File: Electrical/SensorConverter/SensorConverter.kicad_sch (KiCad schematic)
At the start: 35 parts, among them J1 1990067, J2 0430450600, J3 Conn_ARM_SWD_TagConnect_TC203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, U1 THVD1400DR, U2 LP2950CDTX-3.3/NOPB, U3 STM32F103T8U6, U4 M24M01E-FMC6TG

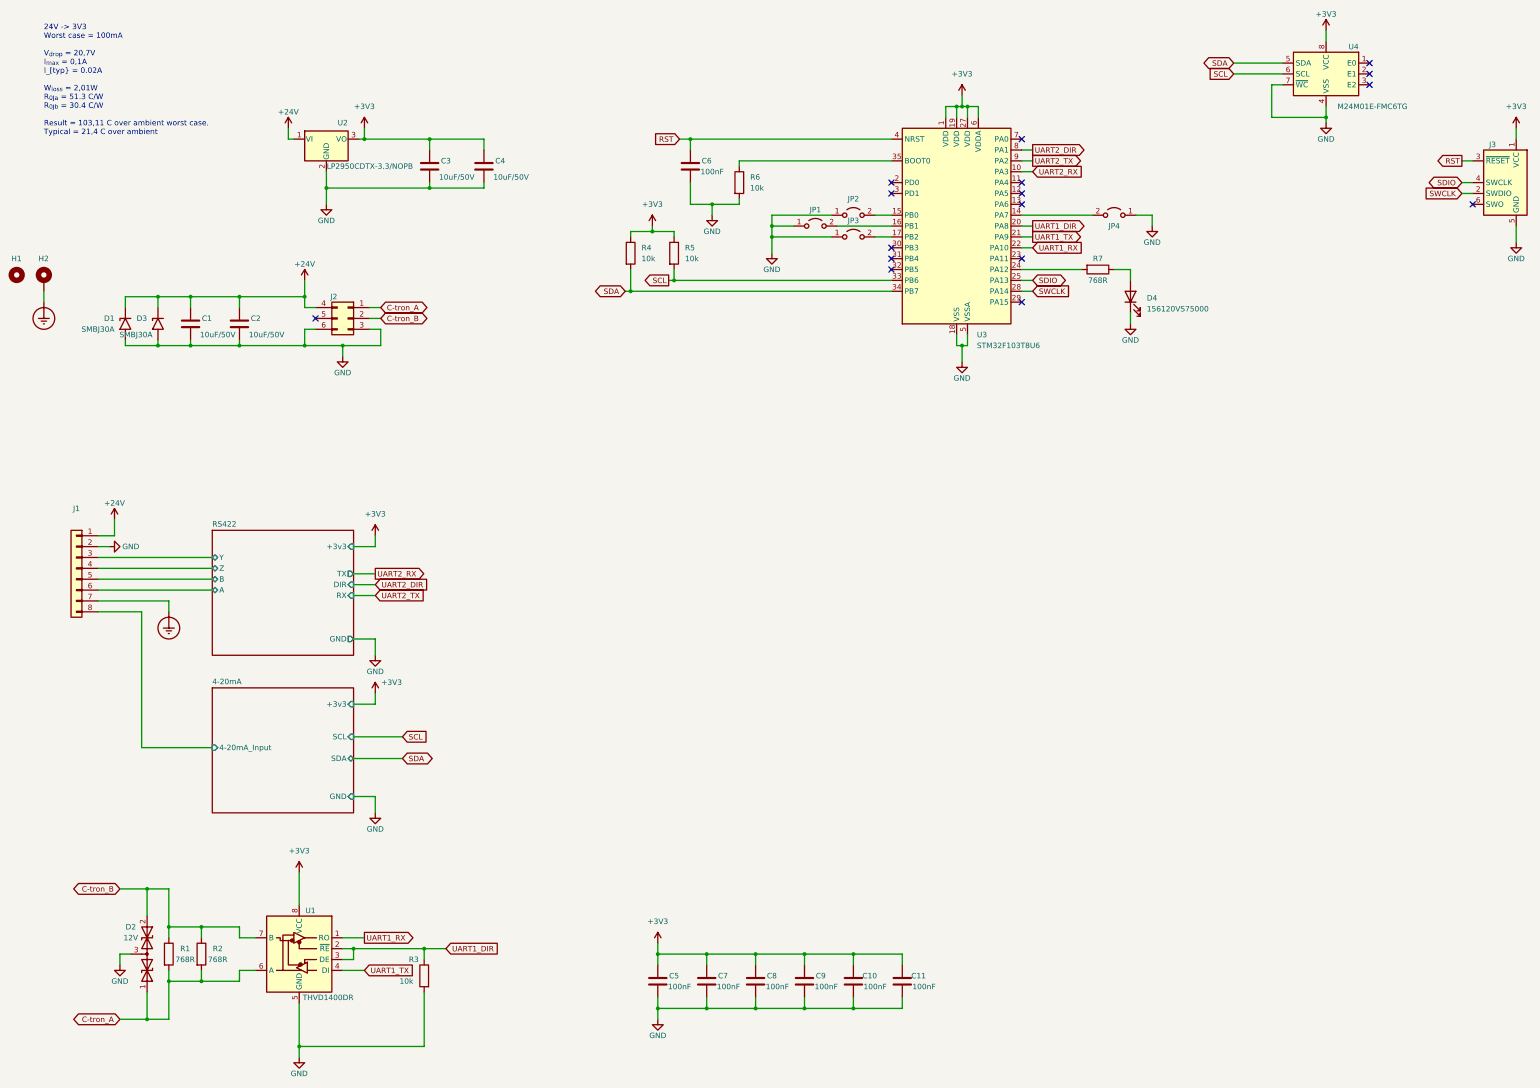
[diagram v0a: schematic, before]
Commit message: Changing processor to STM32G0
This is mostly because of memory constraints and that the F103 is having a lot of issue.
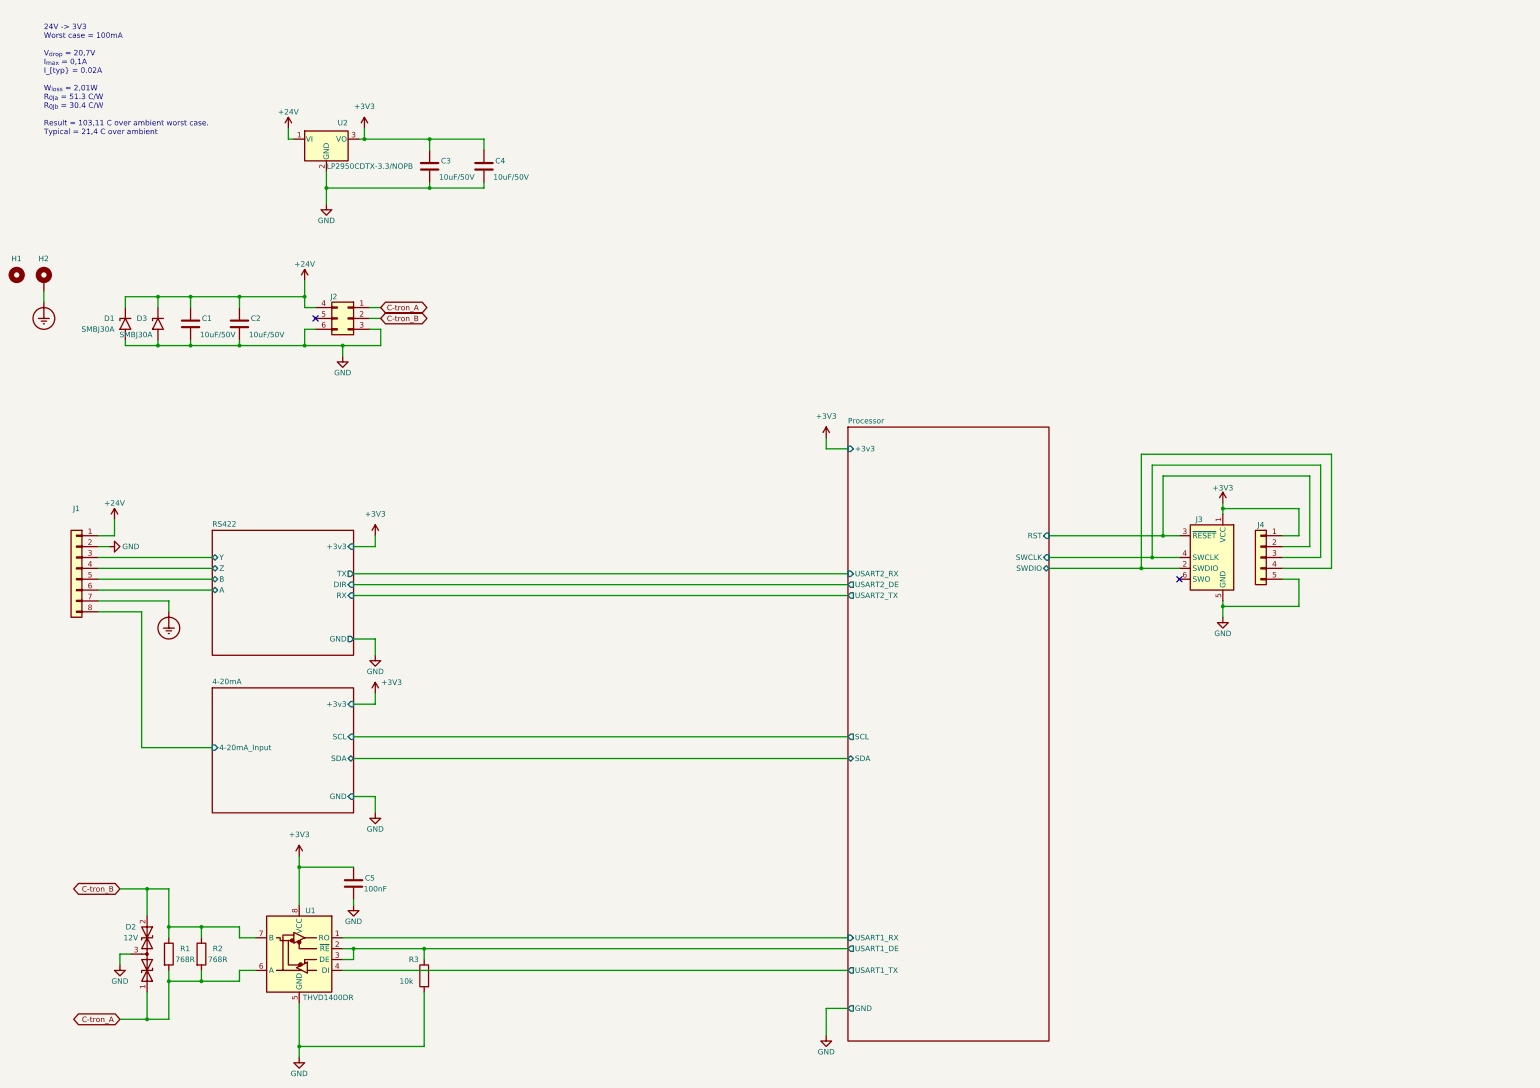
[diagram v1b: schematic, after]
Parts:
- removed C10, C11, C6, C7, C8, C9: 100nF, Capacitor_SMD:C_0402_1005Metric, symbol Device:C
- removed D4: 156120VS75000, LT600_Adapter:WL-SMRW, symbol Device:LED
- removed JP1, JP2, JP3, JP4: Jumper_2_Open, Jumper:SolderJumper-2_P1.3mm_Open_RoundedPad1.0x1.5mm, symbol Jumper:Jumper_2_Open
- removed R4, R5, R6: 10k, Resistor_SMD:R_0402_1005Metric, symbol Device:R
- removed R7: 768R, Resistor_SMD:R_0603_1608Metric, symbol Device:R
- removed U3: STM32F103T8U6, Package_DFN_QFN:QFN-36-1EP_6x6mm_P0.5mm_EP4.1x4.1mm, symbol MCU_ST_STM32F1:STM32F103T8Ux
- removed U4: M24M01E-FMC6TG, Package_DFN_QFN:DFN-8-1EP_3x2mm_P0.5mm_EP1.3x1.5mm, symbol Memory_EEPROM:M24C01-FMN
- added J4: Conn_01x05, Connector_PinHeader_1.27mm:PinHeader_1x05_P1.27mm_Vertical, symbol Connector_Generic:Conn_01x05
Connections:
- net +3V3: now also J4.1 (Pin_1)
- net GND: now also J4.5 (Pin_5)
- net RST renamed Processor/RST
- net Processor/RST: now also J4.2 (Pin_2)
- net SDIO renamed Processor/SWCLK
- net Processor/SWCLK: now also J4.3 (Pin_3)
- net SWCLK renamed Processor/SWDIO
- net Processor/SWDIO: now also J4.4 (Pin_4)
- net UART1_DIR renamed Processor/USART1_DE
- net UART1_RX renamed Processor/USART1_RX
- net UART1_TX renamed Processor/USART1_TX
- no-connect marks 16 -> 2
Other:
- added sheet Processor (STM32G0.kicad_sch)
- moved on the sheet: C5, J3

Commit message: Finalized PCB RevB
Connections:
- net Processor/SWCLK: now also J4.4 (Pin_4); no longer J4.3 (Pin_3)
- net Processor/SWDIO: now also J4.3 (Pin_3); no longer J4.4 (Pin_4)
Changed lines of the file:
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@@
+	)
+	(junction
+		(at 295.91 144.78)
+		(diameter 0)
+		(color 0 0 0 0)
 	)
 	(junction
@@
 	)
 	(junction
+		(at 298.45 147.32)
+		(diameter 0)
+		(color 0 0 0 0)
+	)
+	(junction
 		(at 68.58 231.14)
 		(diameter 0)
@@
 	(junction
 		(at 109.22 95.25)
-		(diameter 0)
-		(color 0 0 0 0)
-	)
-	(junction
-		(at 298.45 144.78)
-		(diameter 0)
-		(color 0 0 0 0)
-	)
-	(junction
-		(at 295.91 147.32)
 		(diameter 0)
 		(color 0 0 0 0)
@@
 	(wire
 		(pts
-			(xy 274.32 144.78) (xy 298.45 144.78)
+			(xy 274.32 144.78) (xy 295.91 144.78)
+		)
+		(stroke
+			(width 0)
+			(type default)
+		)
+	)
+	(wire
+		(pts
+			(xy 295.91 120.65) (xy 295.91 144.78)
 		)
 		(stroke
@@
 	(wire
 		(pts
-			(xy 295.91 120.65) (xy 295.91 147.32)
-		)
-		(stroke
-			(width 0)
-			(type default)
-		)
-	)
-	(wire
-		(pts
 			(xy 68.58 243.84) (xy 76.2 243.84)
 		)
@@
 	(wire
 		(pts
-			(xy 274.32 147.32) (xy 295.91 147.32)
-		)
-		(stroke
-			(width 0)
-			(type default)
-		)
-	)
-	(wire
-		(pts
 			(xy 335.28 142.24) (xy 335.28 125.73)
 		)
@@
 	(wire
 		(pts
-			(xy 298.45 144.78) (xy 304.8 144.78)
-		)
-		(stroke
-			(width 0)
-			(type default)
-		)
-	)
-	(wire
-		(pts
 			(xy 109.22 95.25) (xy 109.22 97.79)
 		)
@@
 	(wire
 		(pts
-			(xy 295.91 147.32) (xy 304.8 147.32)
+			(xy 274.32 147.32) (xy 298.45 147.32)
 		)
 		(stroke
@@
 	(wire
 		(pts
+			(xy 298.45 147.32) (xy 304.8 147.32)
+		)
+		(stroke
+			(width 0)
+			(type default)
+		)
+	)
+	(wire
+		(pts
 			(xy 328.93 149.86) (xy 332.74 149.86)
 		)
@@
 	(wire
 		(pts
-			(xy 298.45 144.78) (xy 298.45 123.19)
-		)
-		(stroke
-			(width 0)
-			(type default)
-		)
-	)
-	(wire
-		(pts
 			(xy 39.37 82.55) (xy 39.37 85.09)
 		)
@@
 	(wire
 		(pts
+			(xy 298.45 123.19) (xy 298.45 147.32)
+		)
+		(stroke
+			(width 0)
+			(type default)
+		)
+	)
+	(wire
+		(pts
 			(xy 97.79 46.99) (xy 96.52 46.99)
 		)
@@
 		)
 		(stroke
+			(width 0)
+			(type default)
+		)
+	)
+	(wire
+		(pts
+			(xy 295.91 144.78) (xy 304.8 144.78)
+		)
+		(stroke

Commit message: WIP
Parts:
- removed J4: Conn_01x05, Connector_PinHeader_1.27mm:PinHeader_1x05_P1.27mm_Vertical, symbol Connector_Generic:Conn_01x05
